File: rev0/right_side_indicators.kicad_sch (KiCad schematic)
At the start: 26 parts, among them IC1 ECP5-BGA256, U14 74AUP2G126, U2 74AUP2G126

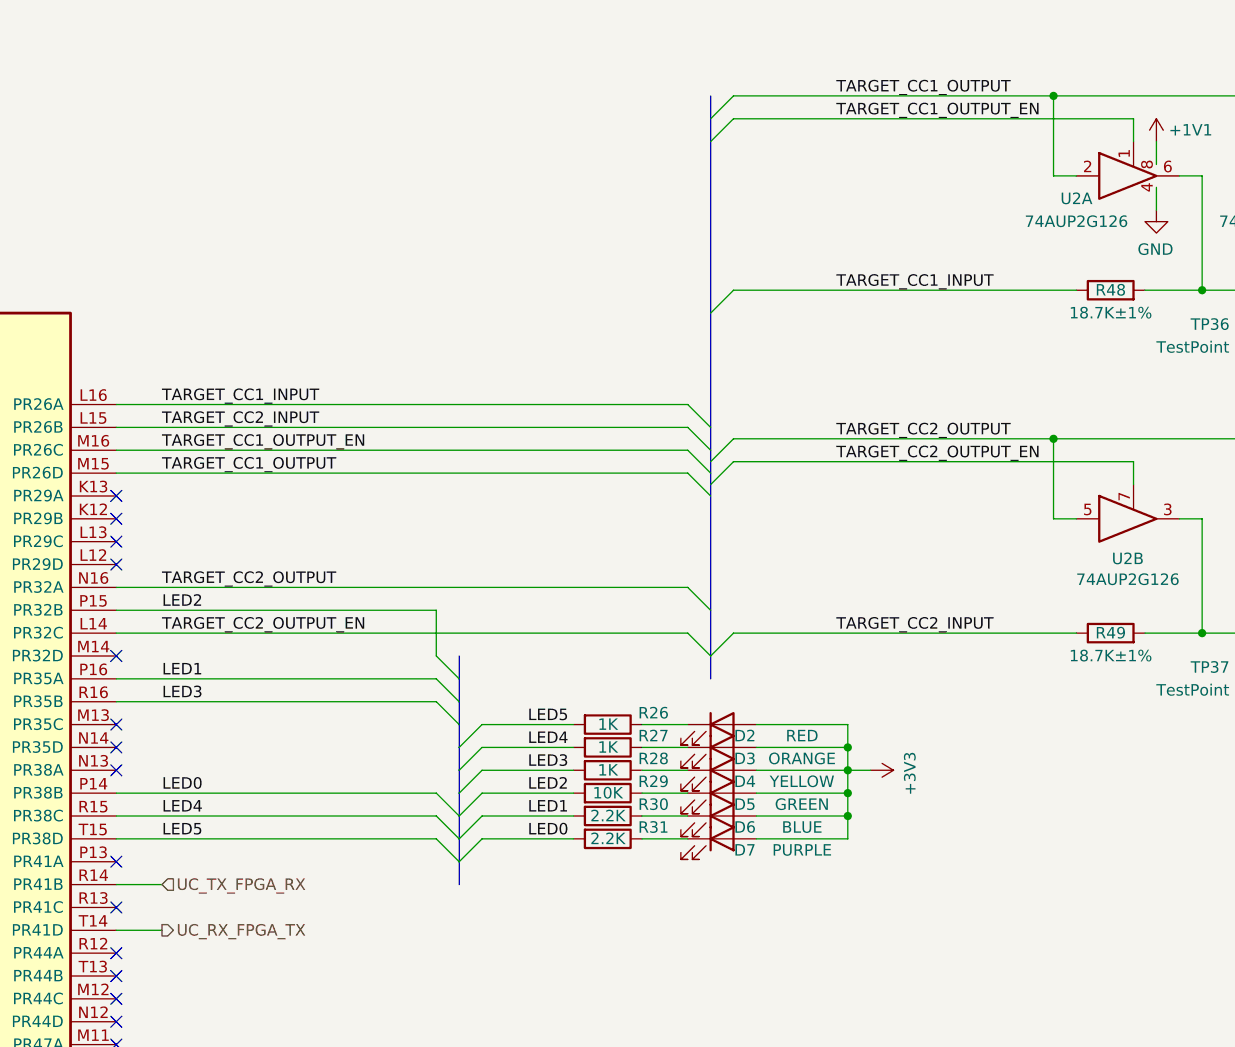
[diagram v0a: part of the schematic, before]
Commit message: hardware: rename buses for KiCad 6
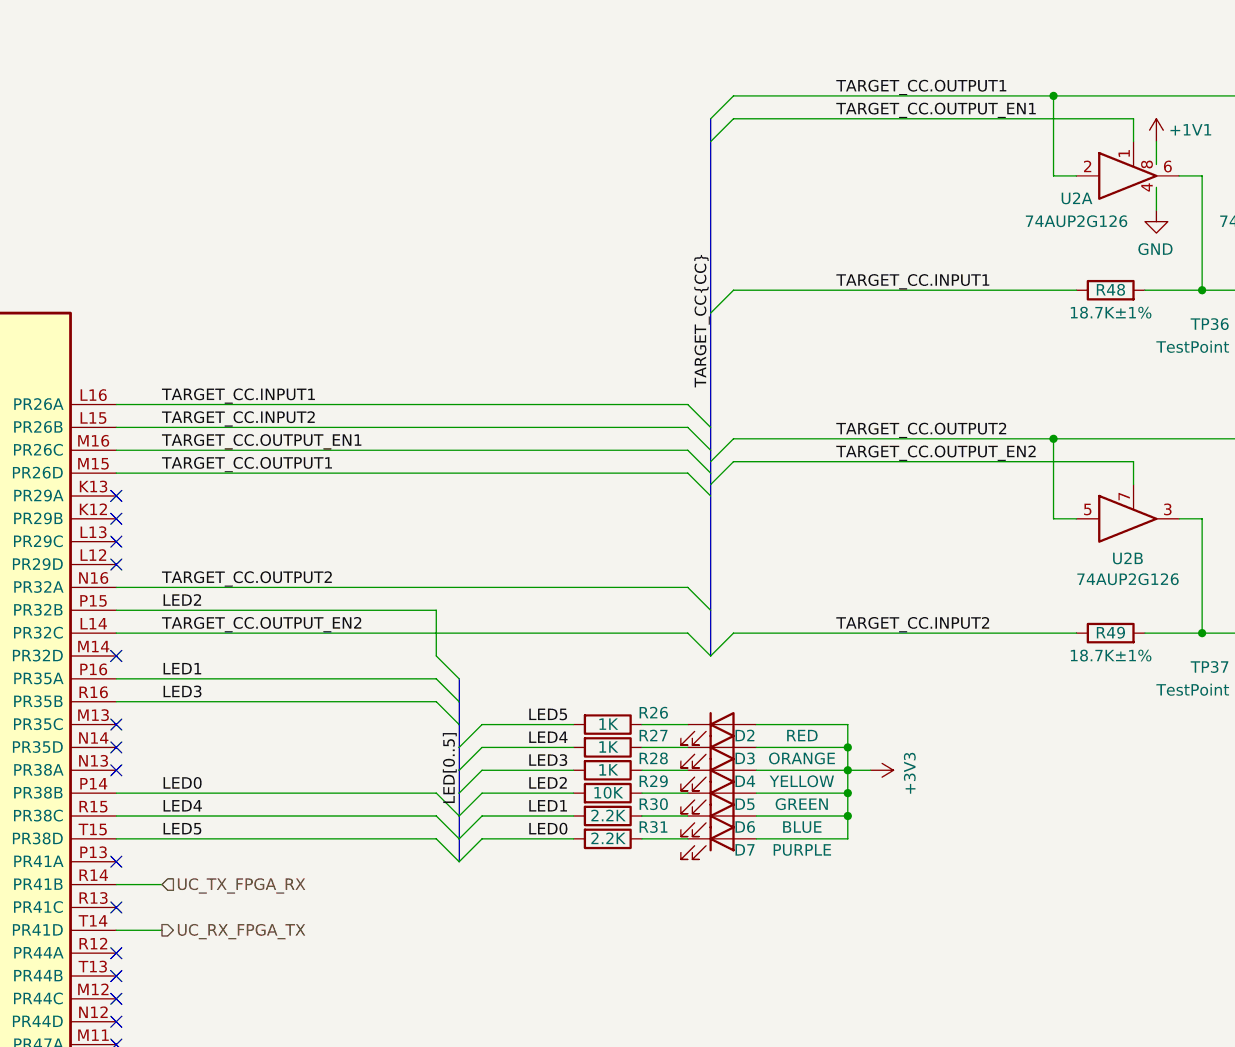
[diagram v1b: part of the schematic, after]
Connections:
- net TARGET_CC1_INPUT renamed TARGET_CC.INPUT1
- net TARGET_CC1_OUTPUT renamed TARGET_CC.OUTPUT1
- net TARGET_CC1_OUTPUT_EN renamed TARGET_CC.OUTPUT_EN1
- net TARGET_CC2_INPUT renamed TARGET_CC.INPUT2
- net TARGET_CC2_OUTPUT renamed TARGET_CC.OUTPUT2
- net TARGET_CC2_OUTPUT_EN renamed TARGET_CC.OUTPUT_EN2
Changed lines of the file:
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@@
     (comment 1 "Licensed under the CERN-OHL-P v2")
   )
+  (bus_alias "CC" (members "INPUT[1..2]" "OUTPUT[1..2]" "OUTPUT_EN[1..2]"))
   (junction (at 201.93 88.9) (diameter 0) (color 0 0 0 0)
   )
@@
     (stroke (width 0) (type default) (color 0 0 0 0))
   )
-  (bus (pts (xy 142.24 29.21) (xy 142.24 31.75))
-    (stroke (width 0) (type default) (color 0 0 0 0))
-  )
   (wire (pts (xy 157.48 104.14) (xy 160.02 104.14))
     (stroke (width 0) (type default) (color 0 0 0 0))
@@
     (stroke (width 0) (type default) (color 0 0 0 0))
   )
-  (bus (pts (xy 114.3 91.44) (xy 114.3 93.98))
-    (stroke (width 0) (type default) (color 0 0 0 0))
-  )
   (wire (pts (xy 213.36 99.06) (xy 213.36 101.6))
     (stroke (width 0) (type default) (color 0 0 0 0))
@@
     (stroke (width 0) (type default) (color 0 0 0 0))
   )
-  (bus (pts (xy 142.24 91.44) (xy 142.24 93.98))
-    (stroke (width 0) (type default) (color 0 0 0 0))
-  )
   (wire (pts (xy 191.77 39.37) (xy 191.77 41.91))
     (stroke (width 0) (type default) (color 0 0 0 0))
@@
   )
   (wire (pts (xy 76.2 93.98) (xy 111.76 93.98))
-    (stroke (width 0) (type default) (color 0 0 0 0))
-  )
-  (bus (pts (xy 114.3 114.3) (xy 114.3 116.84))
     (stroke (width 0) (type default) (color 0 0 0 0))
   )
@@
     (effects (font (size 1.27 1.27)) (justify left bottom))
   )
-  (label "TARGET_CC2_OUTPUT_EN" (at 156.21 69.85 0)
-    (effects (font (size 1.27 1.27)) (justify left bottom))
-  )
-  (label "TARGET_CC2_OUTPUT" (at 156.21 67.31 0)
-    (effects (font (size 1.27 1.27)) (justify left bottom))
-  )
-  (label "TARGET_CC1_OUTPUT_EN" (at 81.28 68.58 0)
-    (effects (font (size 1.27 1.27)) (justify left bottom))
-  )
-  (label "TARGET_CC1_INPUT" (at 81.28 63.5 0)
-    (effects (font (size 1.27 1.27)) (justify left bottom))
-  )
-  (label "TARGET_CC1_INPUT" (at 156.21 50.8 0)
+  (label "TARGET_CC.OUTPUT_EN2" (at 156.21 69.85 0)
+    (effects (font (size 1.27 1.27)) (justify left bottom))
+  )
+  (label "TARGET_CC.OUTPUT2" (at 156.21 67.31 0)
+    (effects (font (size 1.27 1.27)) (justify left bottom))
+  )
+  (label "TARGET_CC.OUTPUT_EN1" (at 81.28 68.58 0)
+    (effects (font (size 1.27 1.27)) (justify left bottom))
+  )
+  (label "TARGET_CC.INPUT1" (at 81.28 63.5 0)
+    (effects (font (size 1.27 1.27)) (justify left bottom))
+  )
+  (label "TARGET_CC.INPUT1" (at 156.21 50.8 0)
     (effects (font (size 1.27 1.27)) (justify left bottom))
   )
@@
     (effects (font (size 1.27 1.27)) (justify left bottom))
   )
-  (label "TARGET_CC2_OUTPUT" (at 81.28 83.82 0)
-    (effects (font (size 1.27 1.27)) (justify left bottom))
-  )
-  (label "TARGET_CC1_OUTPUT" (at 81.28 71.12 0)
+  (label "TARGET_CC.OUTPUT2" (at 81.28 83.82 0)
+    (effects (font (size 1.27 1.27)) (justify left bottom))
+  )
+  (label "TARGET_CC.OUTPUT1" (at 81.28 71.12 0)
     (effects (font (size 1.27 1.27)) (justify left bottom))
   )
@@
     (effects (font (size 1.27 1.27)) (justify left bottom))
   )
-  (label "TARGET_CC2_INPUT" (at 81.28 66.04 0)
-    (effects (font (size 1.27 1.27)) (justify left bottom))
-  )
-  (label "TARGET_CC1_OUTPUT" (at 156.21 29.21 0)
+  (label "TARGET_CC.INPUT2" (at 81.28 66.04 0)
+    (effects (font (size 1.27 1.27)) (justify left bottom))
+  )
+  (label "TARGET_CC.OUTPUT1" (at 156.21 29.21 0)
     (effects (font (size 1.27 1.27)) (justify left bottom))
   )
@@
     (effects (font (size 1.27 1.27)) (justify left bottom))
   )
+  (label "LED[0..5]" (at 114.3 107.95 90)
+    (effects (font (size 1.27 1.27)) (justify left bottom))
+  )
   (label "LED3" (at 121.92 104.14 0)
     (effects (font (size 1.27 1.27)) (justify left bottom))
   )
-  (label "TARGET_CC2_OUTPUT_EN" (at 81.28 88.9 0)
-    (effects (font (size 1.27 1.27)) (justify left bottom))
-  )
-  (label "TARGET_CC1_OUTPUT_EN" (at 156.21 31.75 0)
-    (effects (font (size 1.27 1.27)) (justify left bottom))
-  )
-  (label "TARGET_CC2_INPUT" (at 156.21 88.9 0)
+  (label "TARGET_CC.OUTPUT_EN2" (at 81.28 88.9 0)
+    (effects (font (size 1.27 1.27)) (justify left bottom))
+  )
+  (label "TARGET_CC.OUTPUT_EN1" (at 156.21 31.75 0)
+    (effects (font (size 1.27 1.27)) (justify left bottom))
+  )
+  (label "TARGET_CC.INPUT2" (at 156.21 88.9 0)
     (effects (font (size 1.27 1.27)) (justify left bottom))
   )
@@
     (effects (font (size 1.27 1.27)) (justify left bottom))
   )
+  (label "TARGET_CC{CC}" (at 142.24 61.595 90)
+    (effects (font (size 1.27 1.27)) (justify left bottom))
+  )

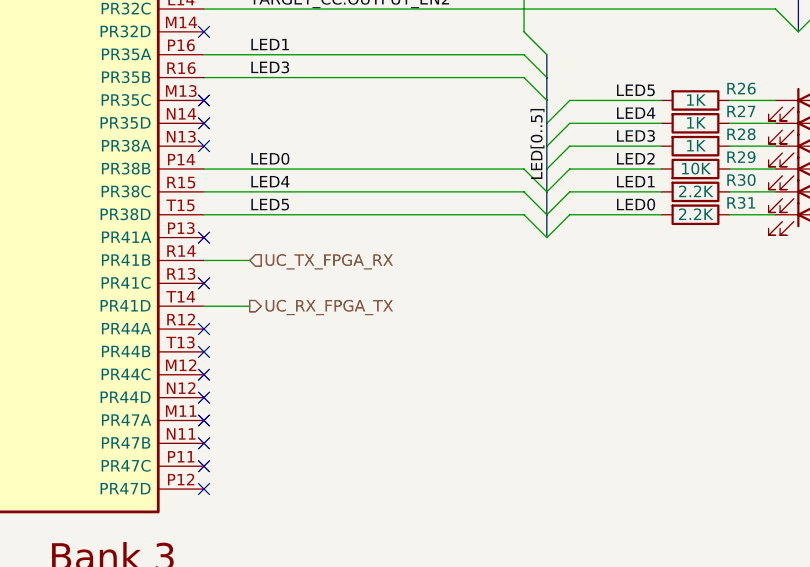
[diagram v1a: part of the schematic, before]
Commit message: hardware: correct or exclude all ERC errors
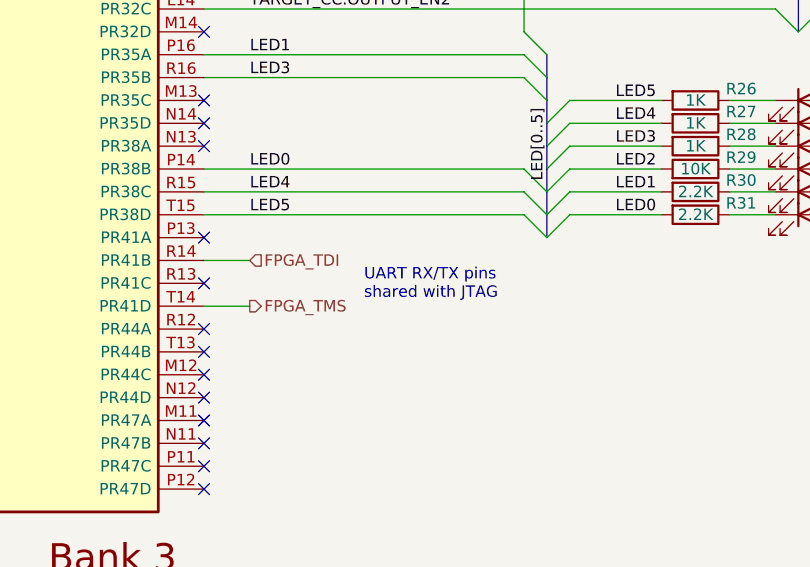
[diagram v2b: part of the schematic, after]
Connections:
- net UC_RX_FPGA_TX renamed FPGA_TMS
- net UC_TX_FPGA_RX renamed FPGA_TDI
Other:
- note added: "UART RX/TX pins shared with JTAG"
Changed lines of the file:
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@@
     (stroke (width 0) (type default) (color 0 0 0 0))
+  )
+  (text "UART RX/TX pins\nshared with JTAG" (at 93.98 121.285 0)
+    (effects (font (size 1.27 1.27)) (justify left bottom))
   )
   (text "high" (at 254 30.48 0)
@@
     (effects (font (size 1.27 1.27)) (justify left))
   )
-  (hierarchical_label "UC_TX_FPGA_RX" (shape input) (at 81.28 116.84 0)
+  (hierarchical_label "FPGA_TDI" (shape input) (at 81.28 116.84 0)
     (effects (font (size 1.27 1.27)) (justify left))
   )
-  (hierarchical_label "UC_RX_FPGA_TX" (shape output) (at 81.28 121.92 0)
+  (hierarchical_label "FPGA_TMS" (shape output) (at 81.28 121.92 0)
     (effects (font (size 1.27 1.27)) (justify left))
   )

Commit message: hardware: use DNP field for DNP notation
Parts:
- TP36, TP37: DNP (none) -> DNP; Note DNP -> (none)
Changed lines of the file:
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@@
       (effects (font (size 1.27 1.27)) hide)
     )
-    (property "Note" "DNP" (id 4) (at 201.93 53.34 0)
+    (property "DNP" "DNP" (id 4) (at 201.93 53.34 0)
       (effects (font (size 1.27 1.27)) hide)
     )
@@
       (effects (font (size 1.27 1.27)) hide)
     )
-    (property "Note" "DNP" (id 4) (at 201.93 91.44 0)
+    (property "DNP" "DNP" (id 4) (at 201.93 91.44 0)
       (effects (font (size 1.27 1.27)) hide)
     )

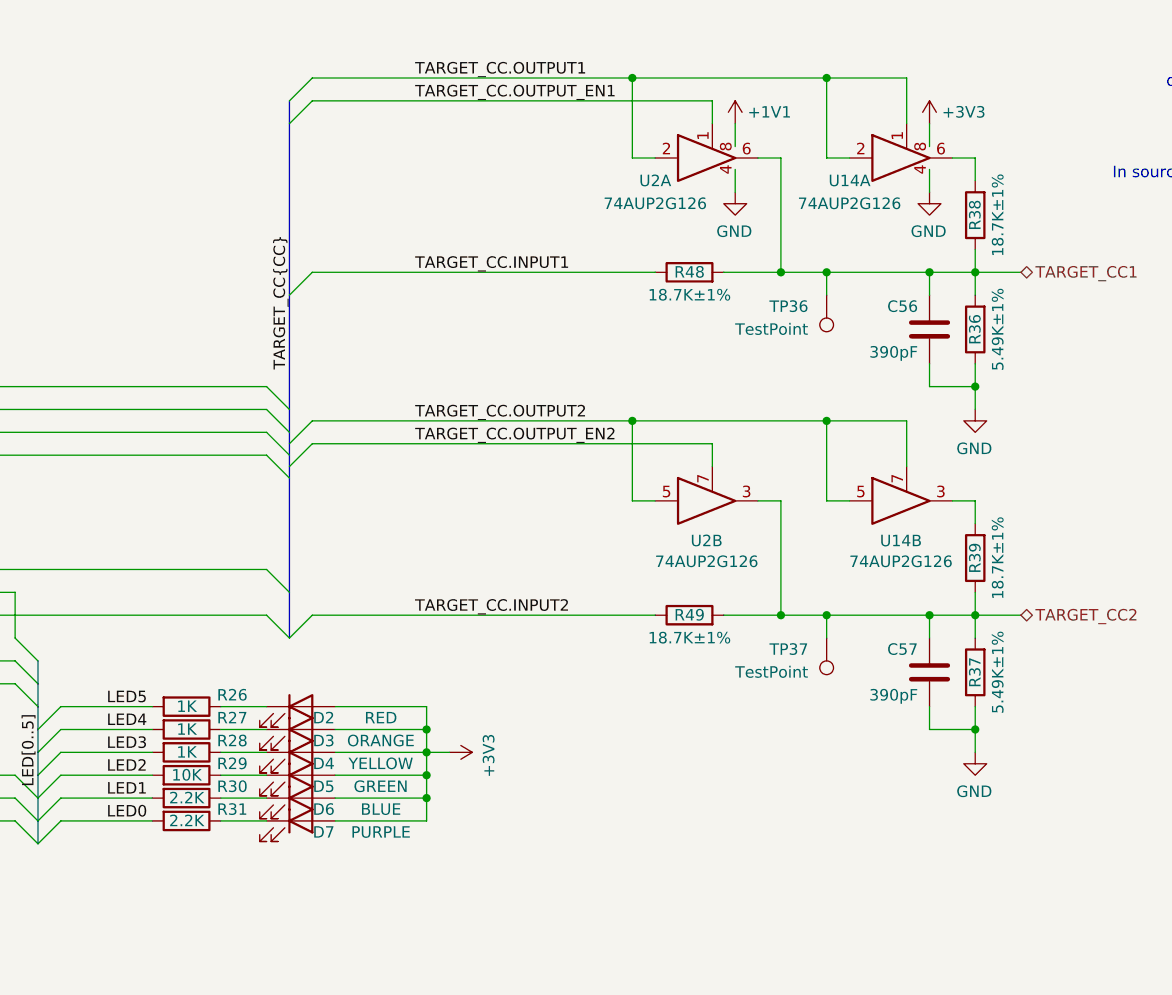
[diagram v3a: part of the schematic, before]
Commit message: hardware: consistently use lowercase k for kilo
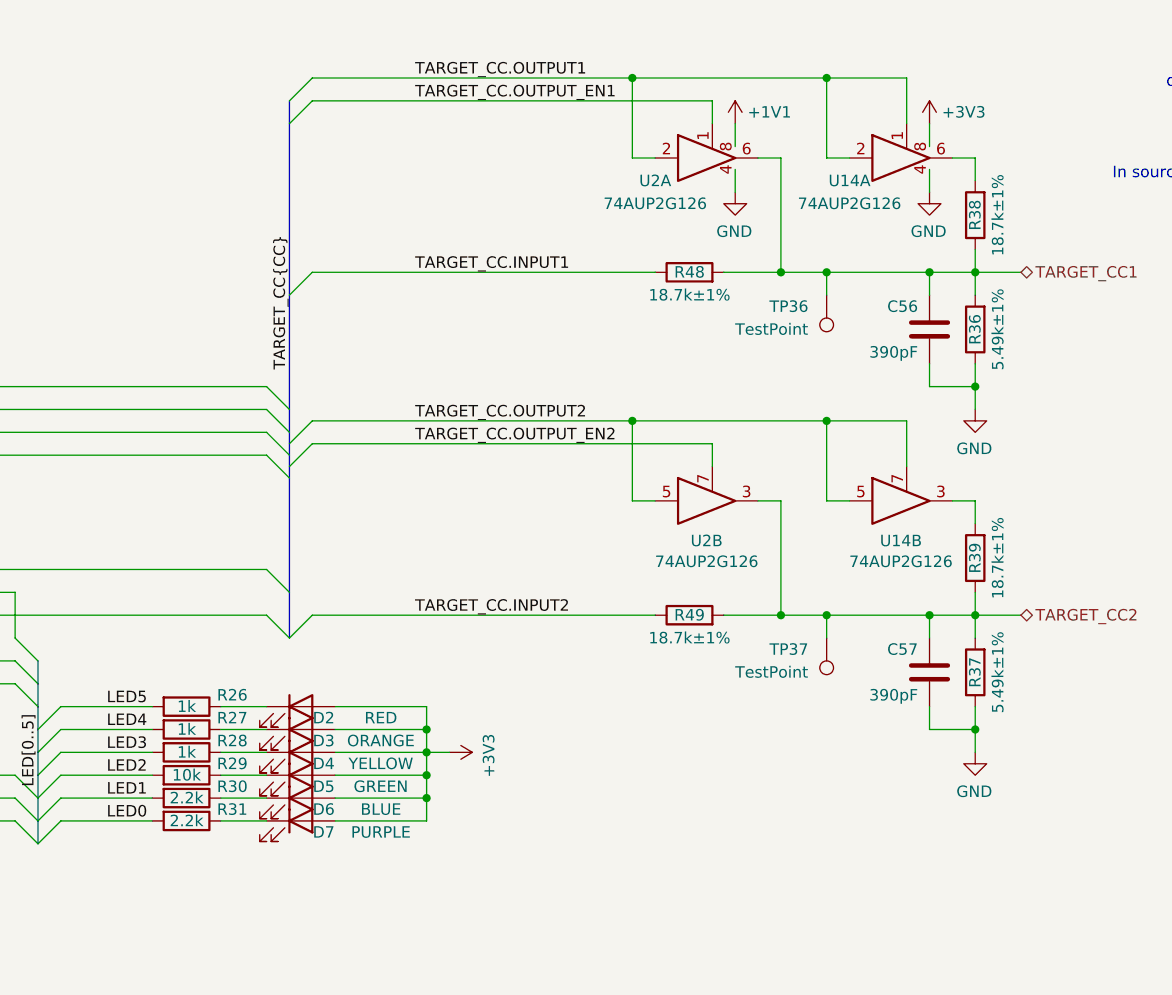
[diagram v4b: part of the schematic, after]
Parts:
- R26, R27, R28: value 1K -> 1k
- R29: value 10K -> 10k
- R30, R31: value 2.2K -> 2.2k
- R36, R37: value 5.49K±1% -> 5.49k±1%
- R38, R39, R48, R49: value 18.7K±1% -> 18.7k±1%
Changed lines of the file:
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@@
     (in_bom yes) (on_board yes)
     (property "Reference" "R29" (id 0) (at 135.89 105.41 90))
-    (property "Value" "10K" (id 1) (at 130.81 106.68 90))
+    (property "Value" "10k" (id 1) (at 130.81 106.68 90))
     (property "Footprint" "Resistor_SMD:R_0402_1005Metric" (id 2) (at 130.81 108.458 90)
       (effects (font (size 1.27 1.27)) hide)
@@
     (in_bom yes) (on_board yes)
     (property "Reference" "R30" (id 0) (at 135.89 107.95 90))
-    (property "Value" "2.2K" (id 1) (at 130.81 109.22 90))
+    (property "Value" "2.2k" (id 1) (at 130.81 109.22 90))
     (property "Footprint" "Resistor_SMD:R_0402_1005Metric" (id 2) (at 130.81 107.442 90)
       (effects (font (size 1.27 1.27)) hide)
@@
     (in_bom yes) (on_board yes)
     (property "Reference" "R31" (id 0) (at 135.89 110.49 90))
-    (property "Value" "2.2K" (id 1) (at 130.81 111.76 90))
+    (property "Value" "2.2k" (id 1) (at 130.81 111.76 90))
     (property "Footprint" "Resistor_SMD:R_0402_1005Metric" (id 2) (at 130.81 109.982 90)
       (effects (font (size 1.27 1.27)) hide)
@@
     (in_bom yes) (on_board yes)
     (property "Reference" "R49" (id 0) (at 186.69 88.9 90))
-    (property "Value" "18.7K±1%" (id 1) (at 186.69 91.44 90))
+    (property "Value" "18.7k±1%" (id 1) (at 186.69 91.44 90))
     (property "Footprint" "Resistor_SMD:R_0402_1005Metric" (id 2) (at 186.69 90.678 90)
       (effects (font (size 1.27 1.27)) hide)
@@
     (in_bom yes) (on_board yes)
     (property "Reference" "R48" (id 0) (at 186.69 50.8 90))
-    (property "Value" "18.7K±1%" (id 1) (at 186.69 53.34 90))
+    (property "Value" "18.7k±1%" (id 1) (at 186.69 53.34 90))
     (property "Footprint" "Resistor_SMD:R_0402_1005Metric" (id 2) (at 186.69 52.578 90)
       (effects (font (size 1.27 1.27)) hide)
@@
     (in_bom yes) (on_board yes)
     (property "Reference" "R36" (id 0) (at 218.44 57.15 90))
-    (property "Value" "5.49K±1%" (id 1) (at 220.98 57.15 90))
+    (property "Value" "5.49k±1%" (id 1) (at 220.98 57.15 90))
     (property "Footprint" "Resistor_SMD:R_0402_1005Metric" (id 2) (at 220.218 57.15 90)
       (effects (font (size 1.27 1.27)) hide)
@@
     (in_bom yes) (on_board yes)
     (property "Reference" "R37" (id 0) (at 218.44 95.25 90))
-    (property "Value" "5.49K±1%" (id 1) (at 220.98 95.25 90))
+    (property "Value" "5.49k±1%" (id 1) (at 220.98 95.25 90))
     (property "Footprint" "Resistor_SMD:R_0402_1005Metric" (id 2) (at 220.218 95.25 90)
       (effects (font (size 1.27 1.27)) hide)
@@
     (in_bom yes) (on_board yes)
     (property "Reference" "R38" (id 0) (at 218.44 44.45 90))
-    (property "Value" "18.7K±1%" (id 1) (at 220.98 44.45 90))
+    (property "Value" "18.7k±1%" (id 1) (at 220.98 44.45 90))
     (property "Footprint" "Resistor_SMD:R_0402_1005Metric" (id 2) (at 220.218 44.45 90)
       (effects (font (size 1.27 1.27)) hide)
@@
     (in_bom yes) (on_board yes)
     (property "Reference" "R39" (id 0) (at 218.44 82.55 90))
-    (property "Value" "18.7K±1%" (id 1) (at 220.98 82.55 90))
+    (property "Value" "18.7k±1%" (id 1) (at 220.98 82.55 90))
     (property "Footprint" "Resistor_SMD:R_0402_1005Metric" (id 2) (at 220.218 82.55 90)
       (effects (font (size 1.27 1.27)) hide)
@@
     (in_bom yes) (on_board yes)
     (property "Reference" "R26" (id 0) (at 135.89 97.79 90))
-    (property "Value" "1K" (id 1) (at 130.81 99.06 90))
+    (property "Value" "1k" (id 1) (at 130.81 99.06 90))
     (property "Footprint" "Resistor_SMD:R_0402_1005Metric" (id 2) (at 130.81 97.282 90)
       (effects (font (size 1.27 1.27)) hide)
@@
     (in_bom yes) (on_board yes)
     (property "Reference" "R27" (id 0) (at 135.89 100.33 90))
-    (property "Value" "1K" (id 1) (at 130.81 101.6 90))
+    (property "Value" "1k" (id 1) (at 130.81 101.6 90))
     (property "Footprint" "Resistor_SMD:R_0402_1005Metric" (id 2) (at 130.81 99.822 90)
       (effects (font (size 1.27 1.27)) hide)
@@
     (in_bom yes) (on_board yes)
     (property "Reference" "R28" (id 0) (at 135.89 102.87 90))
-    (property "Value" "1K" (id 1) (at 130.81 104.14 90))
+    (property "Value" "1k" (id 1) (at 130.81 104.14 90))
     (property "Footprint" "Resistor_SMD:R_0402_1005Metric" (id 2) (at 130.81 102.362 90)
       (effects (font (size 1.27 1.27)) hide)
